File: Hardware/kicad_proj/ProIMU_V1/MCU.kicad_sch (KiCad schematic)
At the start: 8 parts, among them U9 STM32F412CEU6

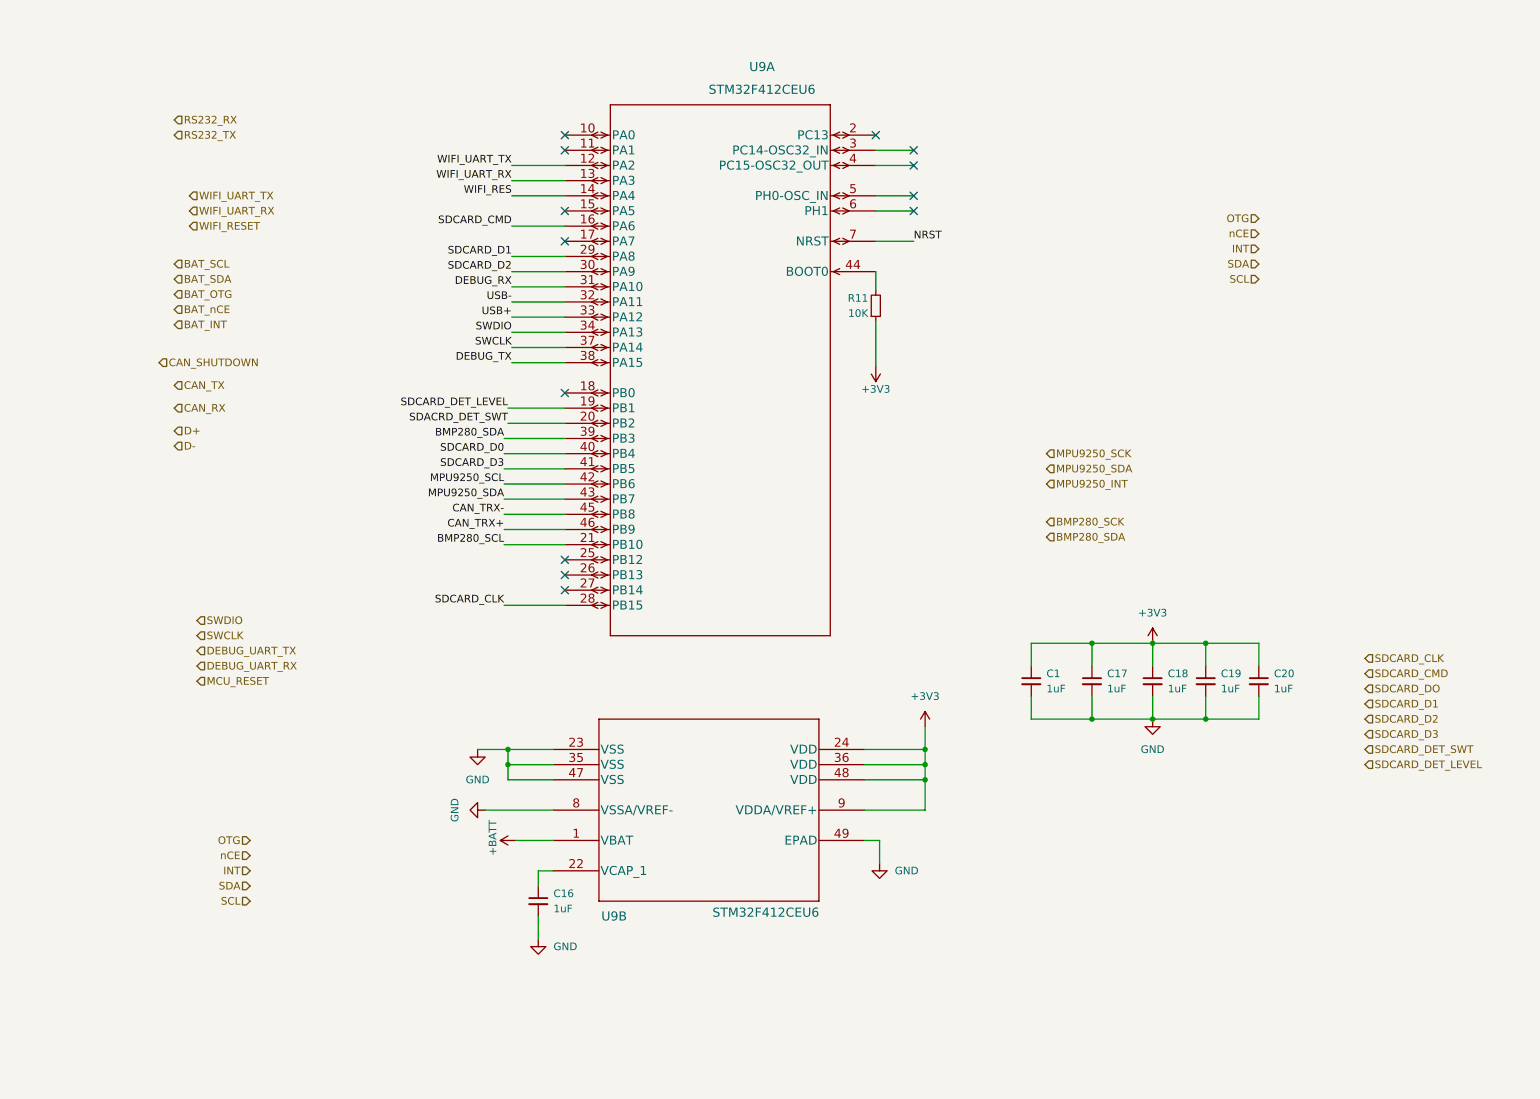
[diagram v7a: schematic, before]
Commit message: Updated Schematic and Layout. RS232 and CAN connectors to be interchanged
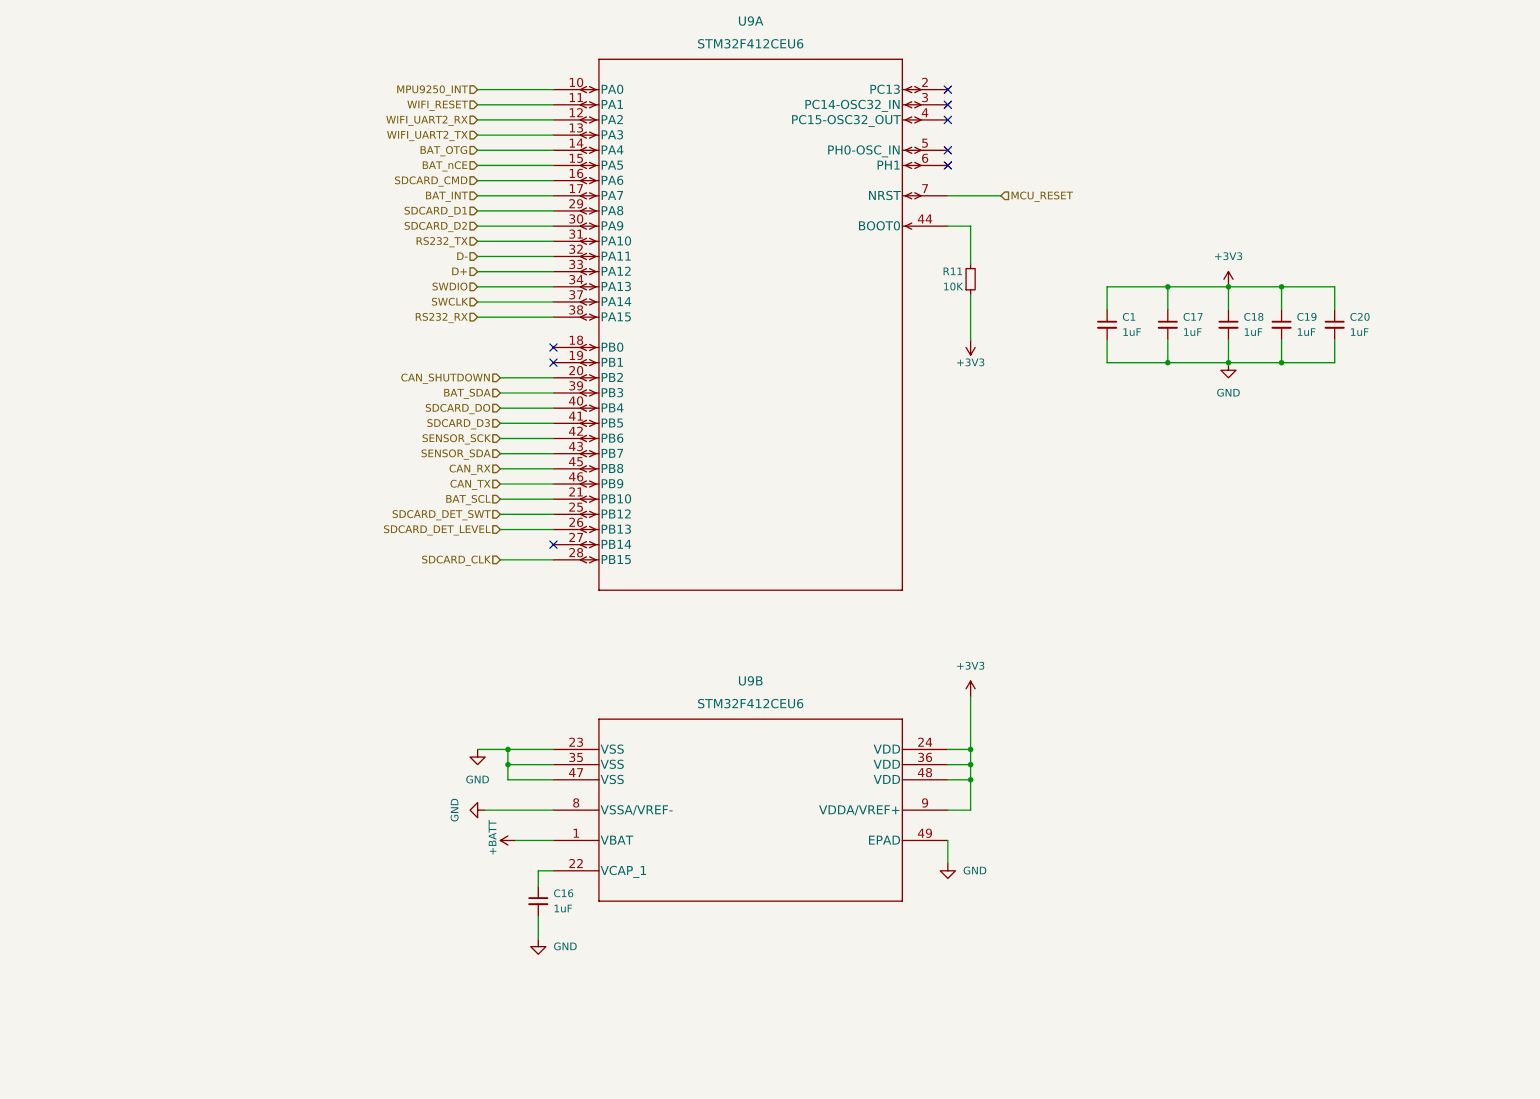
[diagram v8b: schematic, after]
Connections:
- net BMP280_SCL is gone; now on net BAT_SCL: U9.21 (PB10)
- net BMP280_SDA is gone; now on net BAT_SDA: U9.39 (PB3)
- net CAN_TRX+ is gone; now on net CAN_TX: U9.46 (PB9)
- net CAN_TRX- is gone; now on net CAN_RX: U9.45 (PB8)
- net DEBUG_RX is gone; now on net RS232_TX: U9.31 (PA10)
- net DEBUG_TX is gone; now on net RS232_RX: U9.38 (PA15)
- net NRST is gone; now on net MCU_RESET: U9.7 (NRST)
- net SDACRD_DET_SWT is gone; now on net CAN_SHUTDOWN: U9.20 (PB2)
- net SDCARD_D0 is gone; now on net SDCARD_DO: U9.40 (PB4)
- net USB+ is gone; now on net D+: U9.33 (PA12)
- net USB- is gone; now on net D-: U9.32 (PA11)
- net WIFI_RES is gone; now on net BAT_OTG: U9.14 (PA4)
- net BAT_INT: now also U9.17 (PA7)
- net BAT_nCE: now also U9.15 (PA5)
- net MPU9250_INT: now also U9.10 (PA0)
- net SDCARD_DET_LEVEL: now also U9.26 (PB13); no longer U9.19 (PB1)
- net SDCARD_DET_SWT: now also U9.25 (PB12)
- net WIFI_RESET: now also U9.11 (PA1)
- net MPU9250_SCL renamed SENSOR_SCK
- net MPU9250_SDA renamed SENSOR_SDA
- net WIFI_UART_RX renamed WIFI_UART2_TX
- net WIFI_UART_TX renamed WIFI_UART2_RX
- no-connect marks 13 -> 8
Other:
- moved on the sheet: C1, C17, C18, C19, C20, R11
